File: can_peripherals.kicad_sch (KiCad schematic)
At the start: 14 parts, among them U1 MCP2515, U2 MCP2551, Y1 ABLS7M-16.000MHZ-B-2-T

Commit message: footprints
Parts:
- C1, C2: footprint (none) -> Capacitor_SMD:C_0805_2012Metric
- C3: renamed from C9; footprint (none) -> Capacitor_SMD:C_0805_2012Metric
- R3: renamed from R30; footprint (none) -> Resistor_SMD:R_0805_2012Metric
- R4: renamed from R31; value 120 -> R; footprint (none) -> Resistor_SMD:R_0805_2012Metric
- TP1, TP2: footprint (none) -> TestPoint:TestPoint_Pad_D1.5mm
- renumbered JP2 to JP1, JP3 to JP2, JP4 to JP3
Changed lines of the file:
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@@
   (junction (at 208.026 71.882) (diameter 0.9144) (color 0 0 0 0))
   (junction (at 214.376 134.112) (diameter 0.9144) (color 0 0 0 0))
+  (no_connect (at 74.93 44.45))
   (no_connect (at 74.93 41.91))
   (no_connect (at 49.53 52.07))
-  (no_connect (at 74.93 44.45))
   (no_connect (at 49.53 54.61))
+  (no_connect (at 74.93 39.37))
   (no_connect (at 74.93 46.99))
-  (no_connect (at 74.93 39.37))
   (no_connect (at 138.43 39.37))
   (wire (pts (xy 39.37 118.872) (xy 39.37 131.572))
@@
       (effects (font (size 1.27 1.27)) (justify left) hide)
     )
-    (property "Footprint" "" (id 2) (at 46.99 92.202 0)
+    (property "Footprint" "TestPoint:TestPoint_Pad_D1.5mm" (id 2) (at 46.99 92.202 0)
       (effects (font (size 1.27 1.27)) hide)
     )
@@
       (effects (font (size 1.27 1.27)) (justify left) hide)
     )
-    (property "Footprint" "" (id 2) (at 53.34 92.202 0)
+    (property "Footprint" "TestPoint:TestPoint_Pad_D1.5mm" (id 2) (at 53.34 92.202 0)
       (effects (font (size 1.27 1.27)) hide)
     )
@@
   (symbol (lib_id "power:+3.3V") (at 48.26 33.02 0) (unit 1)
     (in_bom yes) (on_board yes)
-    (property "Reference" "#PWR023" (id 0) (at 48.26 36.83 0)
+    (property "Reference" "#PWR0108" (id 0) (at 48.26 36.83 0)
       (effects (font (size 1.27 1.27)) hide)
     )
@@
   (symbol (lib_id "power:+3.3V") (at 110.49 116.332 0) (unit 1)
     (in_bom yes) (on_board yes)
-    (property "Reference" "#PWR027" (id 0) (at 110.49 120.142 0)
+    (property "Reference" "#PWR0113" (id 0) (at 110.49 120.142 0)
       (effects (font (size 1.27 1.27)) hide)
     )
@@
   (symbol (lib_id "power:+5V") (at 115.57 36.83 0) (unit 1)
     (in_bom yes) (on_board yes)
-    (property "Reference" "#PWR025" (id 0) (at 115.57 40.64 0)
+    (property "Reference" "#PWR0111" (id 0) (at 115.57 40.64 0)
       (effects (font (size 1.27 1.27)) hide)
     )
@@
   (symbol (lib_id "power:GND") (at 39.37 134.112 0) (unit 1)
     (in_bom yes) (on_board yes)
-    (property "Reference" "#PWR022" (id 0) (at 39.37 140.462 0)
+    (property "Reference" "#PWR0109" (id 0) (at 39.37 140.462 0)
       (effects (font (size 1.27 1.27)) hide)
     )
@@
   (symbol (lib_id "power:GND") (at 77.47 55.88 0) (unit 1)
     (in_bom yes) (on_board yes)
-    (property "Reference" "#PWR024" (id 0) (at 77.47 62.23 0)
+    (property "Reference" "#PWR0114" (id 0) (at 77.47 62.23 0)
       (effects (font (size 1.27 1.27)) hide)
     )
@@
   (symbol (lib_id "power:GND") (at 110.49 134.112 0) (unit 1)
     (in_bom yes) (on_board yes)
-    (property "Reference" "#PWR028" (id 0) (at 110.49 140.462 0)
+    (property "Reference" "#PWR0112" (id 0) (at 110.49 140.462 0)
       (effects (font (size 1.27 1.27)) hide)
     )
@@
   (symbol (lib_id "power:GND") (at 115.57 49.53 0) (unit 1)
     (in_bom yes) (on_board yes)
-    (property "Reference" "#PWR026" (id 0) (at 115.57 55.88 0)
+    (property "Reference" "#PWR0110" (id 0) (at 115.57 55.88 0)
       (effects (font (size 1.27 1.27)) hide)
     )
@@
   (symbol (lib_id "power:GND") (at 211.836 74.422 0) (unit 1)
     (in_bom yes) (on_board yes)
-    (property "Reference" "#PWR029" (id 0) (at 211.836 80.772 0)
+    (property "Reference" "#PWR0107" (id 0) (at 211.836 80.772 0)
       (effects (font (size 1.27 1.27)) hide)
     )
@@
   (symbol (lib_id "Device:R") (at 110.49 120.142 180) (unit 1)
     (in_bom yes) (on_board yes)
-    (property "Reference" "R30" (id 0) (at 112.2681 118.9926 0)
+    (property "Reference" "R3" (id 0) (at 112.2681 118.9926 0)
       (effects (font (size 1.27 1.27)) (justify right))
     )
@@
       (effects (font (size 1.27 1.27)) (justify right))
     )
-    (property "Footprint" "" (id 2) (at 112.268 120.142 90)
+    (property "Footprint" "Resistor_SMD:R_0805_2012Metric" (id 2) (at 112.268 120.142 90)
       (effects (font (size 1.27 1.27)) hide)
     )
@@
   (symbol (lib_id "Device:R") (at 186.436 134.112 90) (unit 1)
     (in_bom yes) (on_board yes)
-    (property "Reference" "R31" (id 0) (at 186.436 128.8858 90))
-    (property "Value" "120" (id 1) (at 186.436 131.1845 90))
-    (property "Footprint" "" (id 2) (at 186.436 135.89 90)
+    (property "Reference" "R4" (id 0) (at 186.436 128.8858 90))
+    (property "Value" "R" (id 1) (at 186.436 131.1845 90))
+    (property "Footprint" "Resistor_SMD:R_0805_2012Metric" (id 2) (at 186.436 135.89 90)
       (effects (font (size 1.27 1.27)) hide)
     )
@@
   (symbol (lib_id "Jumper:SolderJumper_2_Open") (at 201.676 69.342 180) (unit 1)
     (in_bom yes) (on_board yes)
-    (property "Reference" "JP2" (id 0) (at 201.676 66.3002 0))
+    (property "Reference" "JP1" (id 0) (at 201.676 66.3002 0))
     (property "Value" "SolderJumper_2_Open" (id 1) (at 201.676 76.219 0)
       (effects (font (size 1.27 1.27)) hide)
@@
   (symbol (lib_id "Jumper:SolderJumper_2_Open") (at 204.216 137.922 180) (unit 1)
     (in_bom yes) (on_board yes)
-    (property "Reference" "JP4" (id 0) (at 204.216 141.2302 0))
+    (property "Reference" "JP3" (id 0) (at 204.216 141.2302 0))
     (property "Value" "SolderJumper_2_Open" (id 1) (at 204.216 144.799 0)
       (effects (font (size 1.27 1.27)) hide)
@@
     (property "Reference" "C1" (id 0) (at 48.26 112.5028 90))
     (property "Value" "C" (id 1) (at 48.26 114.8015 90))
-    (property "Footprint" "" (id 2) (at 44.45 117.9068 0)
+    (property "Footprint" "Capacitor_SMD:C_0805_2012Metric" (id 2) (at 44.45 117.9068 0)
       (effects (font (size 1.27 1.27)) hide)
     )
@@
     (property "Reference" "C2" (id 0) (at 45.72 135.3628 90))
     (property "Value" "C" (id 1) (at 48.26 135.1215 90))
-    (property "Footprint" "" (id 2) (at 44.45 130.6068 0)
+    (property "Footprint" "Capacitor_SMD:C_0805_2012Metric" (id 2) (at 44.45 130.6068 0)
       (effects (font (size 1.27 1.27)) hide)
     )
@@
   (symbol (lib_id "Device:C") (at 110.49 130.302 0) (unit 1)
     (in_bom yes) (on_board yes)
-    (property "Reference" "C9" (id 0) (at 113.4111 129.1526 0)
+    (property "Reference" "C3" (id 0) (at 113.4111 129.1526 0)
       (effects (font (size 1.27 1.27)) (justify left))
     )
@@
       (effects (font (size 1.27 1.27)) (justify left))
     )
-    (property "Footprint" "" (id 2) (at 111.4552 134.112 0)
+    (property "Footprint" "Capacitor_SMD:C_0805_2012Metric" (id 2) (at 111.4552 134.112 0)
       (effects (font (size 1.27 1.27)) hide)
     )
@@
   (symbol (lib_id "Device:Jumper") (at 204.216 130.302 0) (unit 1)
     (in_bom yes) (on_board yes)
-    (property "Reference" "JP3" (id 0) (at 204.216 123.7042 0))
+    (property "Reference" "JP2" (id 0) (at 204.216 123.7042 0))
     (property "Value" "Jumper" (id 1) (at 204.216 126.0029 0))
     (property "Footprint" "" (id 2) (at 204.216 130.302 0)

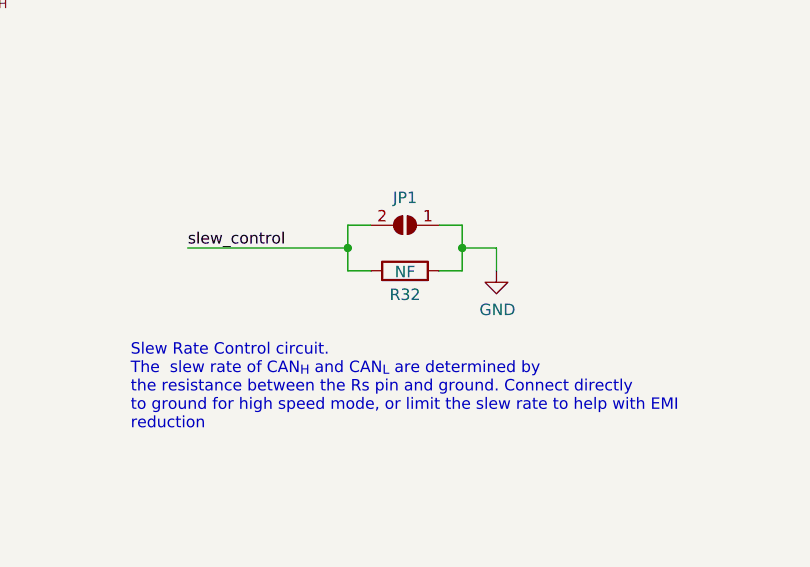
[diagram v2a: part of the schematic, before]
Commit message: Adding footprints and step files for connectors
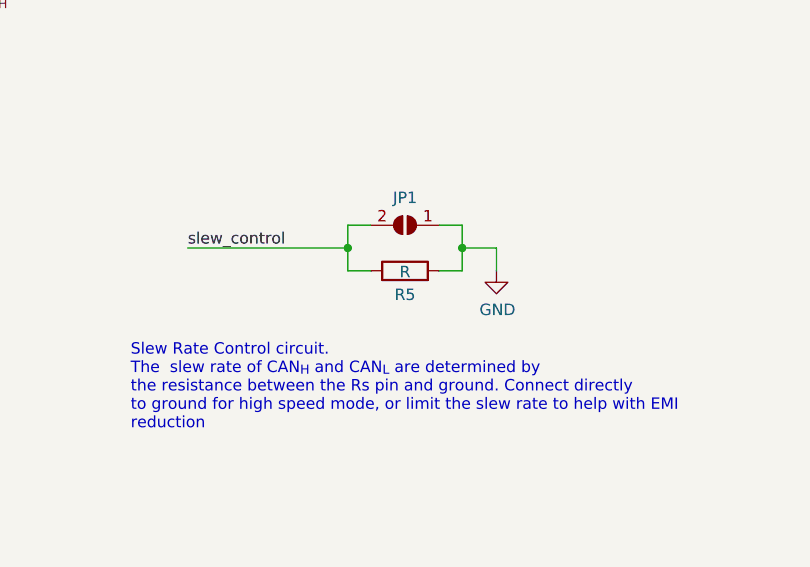
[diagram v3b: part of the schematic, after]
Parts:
- R5: renamed from R32; value NF -> R; footprint (none) -> Resistor_SMD:R_0805_2012Metric
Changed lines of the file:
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@@
   (junction (at 214.376 134.112) (diameter 0.9144) (color 0 0 0 0))
   (no_connect (at 74.93 44.45))
+  (no_connect (at 138.43 39.37))
+  (no_connect (at 49.53 54.61))
+  (no_connect (at 49.53 52.07))
   (no_connect (at 74.93 41.91))
-  (no_connect (at 49.53 52.07))
-  (no_connect (at 49.53 54.61))
+  (no_connect (at 74.93 46.99))
   (no_connect (at 74.93 39.37))
-  (no_connect (at 74.93 46.99))
-  (no_connect (at 138.43 39.37))
   (wire (pts (xy 39.37 118.872) (xy 39.37 131.572))
     (stroke (width 0) (type solid) (color 0 0 0 0))
@@
   (symbol (lib_id "Device:R") (at 201.676 74.422 90) (unit 1)
     (in_bom yes) (on_board yes)
-    (property "Reference" "R32" (id 0) (at 201.676 77.0698 90))
-    (property "Value" "NF" (id 1) (at 201.676 74.5425 90))
-    (property "Footprint" "" (id 2) (at 201.676 76.2 90)
-      (effects (font (size 1.27 1.27)) hide)
-    )
+    (property "Reference" "R5" (id 0) (at 201.676 77.0698 90))
+    (property "Value" "R" (id 1) (at 201.676 74.5425 90))
+    (property "Footprint" "Resistor_SMD:R_0805_2012Metric" (id 2) (at 201.676 76.2 90)
+      (effects (font (size 1.27 1.27)) hide)
+    )

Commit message: footprint assignments
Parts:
- JP1, JP3: footprint (none) -> Jumper:SolderJumper-2_P1.3mm_Open_RoundedPad1.0x1.5mm
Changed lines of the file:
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@@
   (junction (at 208.026 71.882) (diameter 0.9144) (color 0 0 0 0))
   (junction (at 214.376 134.112) (diameter 0.9144) (color 0 0 0 0))
+  (no_connect (at 74.93 41.91))
+  (no_connect (at 138.43 39.37))
+  (no_connect (at 74.93 44.45))
+  (no_connect (at 49.53 54.61))
   (no_connect (at 74.93 46.99))
-  (no_connect (at 138.43 39.37))
-  (no_connect (at 49.53 54.61))
-  (no_connect (at 74.93 41.91))
-  (no_connect (at 74.93 44.45))
   (no_connect (at 74.93 39.37))
   (no_connect (at 49.53 52.07))
@@
   (symbol (lib_id "power:+3.3V") (at 48.26 33.02 0) (unit 1)
     (in_bom yes) (on_board yes)
-    (property "Reference" "#PWR0108" (id 0) (at 48.26 36.83 0)
+    (property "Reference" "#PWR0113" (id 0) (at 48.26 36.83 0)
       (effects (font (size 1.27 1.27)) hide)
     )
@@
   (symbol (lib_id "power:+3.3V") (at 110.49 116.332 0) (unit 1)
     (in_bom yes) (on_board yes)
-    (property "Reference" "#PWR0113" (id 0) (at 110.49 120.142 0)
+    (property "Reference" "#PWR0118" (id 0) (at 110.49 120.142 0)
       (effects (font (size 1.27 1.27)) hide)
     )
@@
   (symbol (lib_id "power:+5V") (at 115.57 36.83 0) (unit 1)
     (in_bom yes) (on_board yes)
-    (property "Reference" "#PWR0111" (id 0) (at 115.57 40.64 0)
+    (property "Reference" "#PWR0116" (id 0) (at 115.57 40.64 0)
       (effects (font (size 1.27 1.27)) hide)
     )
@@
   (symbol (lib_id "power:GND") (at 39.37 134.112 0) (unit 1)
     (in_bom yes) (on_board yes)
-    (property "Reference" "#PWR0109" (id 0) (at 39.37 140.462 0)
+    (property "Reference" "#PWR0114" (id 0) (at 39.37 140.462 0)
       (effects (font (size 1.27 1.27)) hide)
     )
@@
   (symbol (lib_id "power:GND") (at 77.47 55.88 0) (unit 1)
     (in_bom yes) (on_board yes)
-    (property "Reference" "#PWR0114" (id 0) (at 77.47 62.23 0)
+    (property "Reference" "#PWR0119" (id 0) (at 77.47 62.23 0)
       (effects (font (size 1.27 1.27)) hide)
     )
@@
   (symbol (lib_id "power:GND") (at 110.49 134.112 0) (unit 1)
     (in_bom yes) (on_board yes)
-    (property "Reference" "#PWR0112" (id 0) (at 110.49 140.462 0)
+    (property "Reference" "#PWR0117" (id 0) (at 110.49 140.462 0)
       (effects (font (size 1.27 1.27)) hide)
     )
@@
   (symbol (lib_id "power:GND") (at 115.57 49.53 0) (unit 1)
     (in_bom yes) (on_board yes)
-    (property "Reference" "#PWR0110" (id 0) (at 115.57 55.88 0)
+    (property "Reference" "#PWR0115" (id 0) (at 115.57 55.88 0)
       (effects (font (size 1.27 1.27)) hide)
     )
@@
   (symbol (lib_id "power:GND") (at 211.836 74.422 0) (unit 1)
     (in_bom yes) (on_board yes)
-    (property "Reference" "#PWR0107" (id 0) (at 211.836 80.772 0)
+    (property "Reference" "#PWR0112" (id 0) (at 211.836 80.772 0)
       (effects (font (size 1.27 1.27)) hide)
     )
@@
       (effects (font (size 1.27 1.27)) hide)
     )
-    (property "Footprint" "" (id 2) (at 201.676 69.342 0)
+    (property "Footprint" "Jumper:SolderJumper-2_P1.3mm_Open_RoundedPad1.0x1.5mm" (id 2) (at 201.676 69.342 0)
       (effects (font (size 1.27 1.27)) hide)
     )
@@
       (effects (font (size 1.27 1.27)) hide)
     )
-    (property "Footprint" "" (id 2) (at 204.216 137.922 0)
-      (effects (font (size 1.27 1.27)) hide)
-    )
+    (property "Footprint" "Jumper:SolderJumper-2_P1.3mm_Open_RoundedPad1.0x1.5mm" (id 2) (at 204.216 137.922 0)
+      (effects (font (size 1.27 1.27)) hide)
+    )

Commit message: Added Daughter Card
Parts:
- JP2: footprint (none) -> Connector_PinHeader_2.54mm:PinHeader_1x02_P2.54mm_Vertical
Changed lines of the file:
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@@
   (title_block
     (title "Dennis")
-    (date "2020-12-31")
-    (rev "0.1.1")
+    (date "2021-02-26")
+    (rev "0.1.2")
     (company "eCafe Racer")
   )
@@
   (junction (at 208.026 71.882) (diameter 0.9144) (color 0 0 0 0))
   (junction (at 214.376 134.112) (diameter 0.9144) (color 0 0 0 0))
+  (no_connect (at 138.43 39.37))
   (no_connect (at 74.93 41.91))
+  (no_connect (at 74.93 46.99))
+  (no_connect (at 74.93 39.37))
+  (no_connect (at 49.53 52.07))
   (no_connect (at 74.93 44.45))
-  (no_connect (at 49.53 52.07))
-  (no_connect (at 138.43 39.37))
   (no_connect (at 49.53 54.61))
-  (no_connect (at 74.93 39.37))
-  (no_connect (at 74.93 46.99))
   (wire (pts (xy 39.37 118.872) (xy 39.37 131.572))
     (stroke (width 0) (type solid) (color 0 0 0 0))
@@
     (property "Reference" "JP2" (id 0) (at 204.216 123.7042 0))
     (property "Value" "Jumper" (id 1) (at 204.216 126.0029 0))
-    (property "Footprint" "" (id 2) (at 204.216 130.302 0)
-      (effects (font (size 1.27 1.27)) hide)
-    )
+    (property "Footprint" "Connector_PinHeader_2.54mm:PinHeader_1x02_P2.54mm_Vertical" (id 2) (at 204.216 130.302 0)
+      (effects (font (size 1.27 1.27)) hide)
+    )
